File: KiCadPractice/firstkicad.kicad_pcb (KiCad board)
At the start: 2 copper layers, 207 x 115.5 mm, 12 parts, among them Q1 BC337, U1 LM358, U2 LM358

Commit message: Fixed edge-cuts.
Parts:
- removed the U1 at (191.5, 99.5)
- C1: footprint Capacitor_THT:CP_Axial_L30.0mm_D18.0mm_P35.00mm_Horizontal -> Capacitor_SMD:C_1206_3216Metric_Pad1.33x1.80mm_HandSolder
- D1: value D_Photo -> LTR-516AD; footprint Diode_THT:D_A-405_P5.08mm_Vertical_KathodeUp -> Library:LTR-516AD
- Q1: footprint Transformer_THT:Autotransformer_Toroid_1Tap_Horizontal_D10.5mm_Amidon-T37 -> Package_TO_SOT_THT:TO-92_Inline
- R1, R2, R3, R4, R6: footprint Resistor_THT:R_Axial_DIN0204_L3.6mm_D1.6mm_P7.62mm_Horizontal -> Resistor_SMD:R_1206_3216Metric_Pad1.30x1.75mm_HandSolder
- U1: renamed from U2; footprint OptoDevice:Broadcom_APDS-9160-003 -> Package_TO_SOT_SMD:SOT-23-8_Handsoldering
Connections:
- D1 pad 1: 5 -> +5V
- R2 pad 1: 5 -> +5V
- R3 pad 1: 5 -> +5V
- R6 pad 1: 5 -> +5V
- RV1 pad 2: Net-(U2A--) -> Net-(U1B--)
- RV2 pad 2: Net-(U2A-+) -> Net-(U1B-+)
- U1 pad 1: Net-(RV1-Pad3) -> Net-(U1A--)
- U1 pad 2: Net-(U2A--) -> Net-(U1A--)
- U1 pad 3: Net-(U2A-+) -> Net-(U1A-+)
- U1 pad 4: (no net) -> +5V
- U1 pad 5: (no net) -> Net-(U1B-+)
- U1 pad 6: (no net) -> Net-(U1B--)
- U1 pad 7: (no net) -> Net-(RV1-Pad3)
- U1 pad 8: (no net) -> GND
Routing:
- net Net-(U1A--): track 29.4 -> 101.0 mm
- net Net-(U1A-+): track 71.6 -> 0.00 mm
- net Net-(U2A-+): track 69.2 -> 0.00 mm
- net (no net): track 0.00 -> 69.2 mm
- net Net-(U2A--): track 22.3 -> 0.00 mm
- net Net-(U1B--): track 0.00 -> 22.3 mm
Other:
- board size 207 x 115.5 mm -> 196.2 x 103 mm

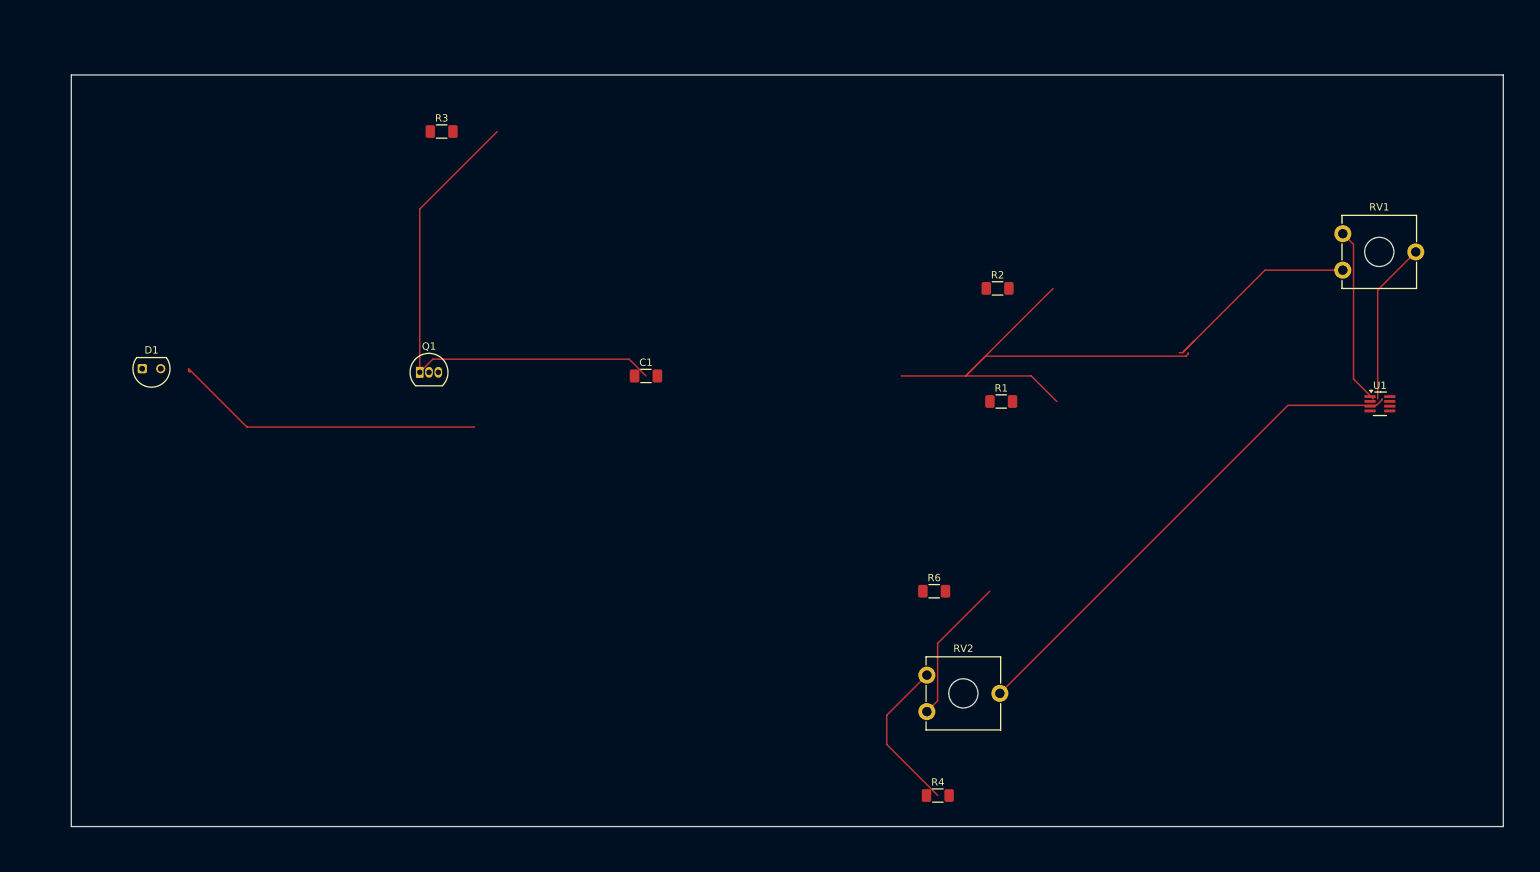
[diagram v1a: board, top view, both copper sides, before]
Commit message: Patched some more footprints.
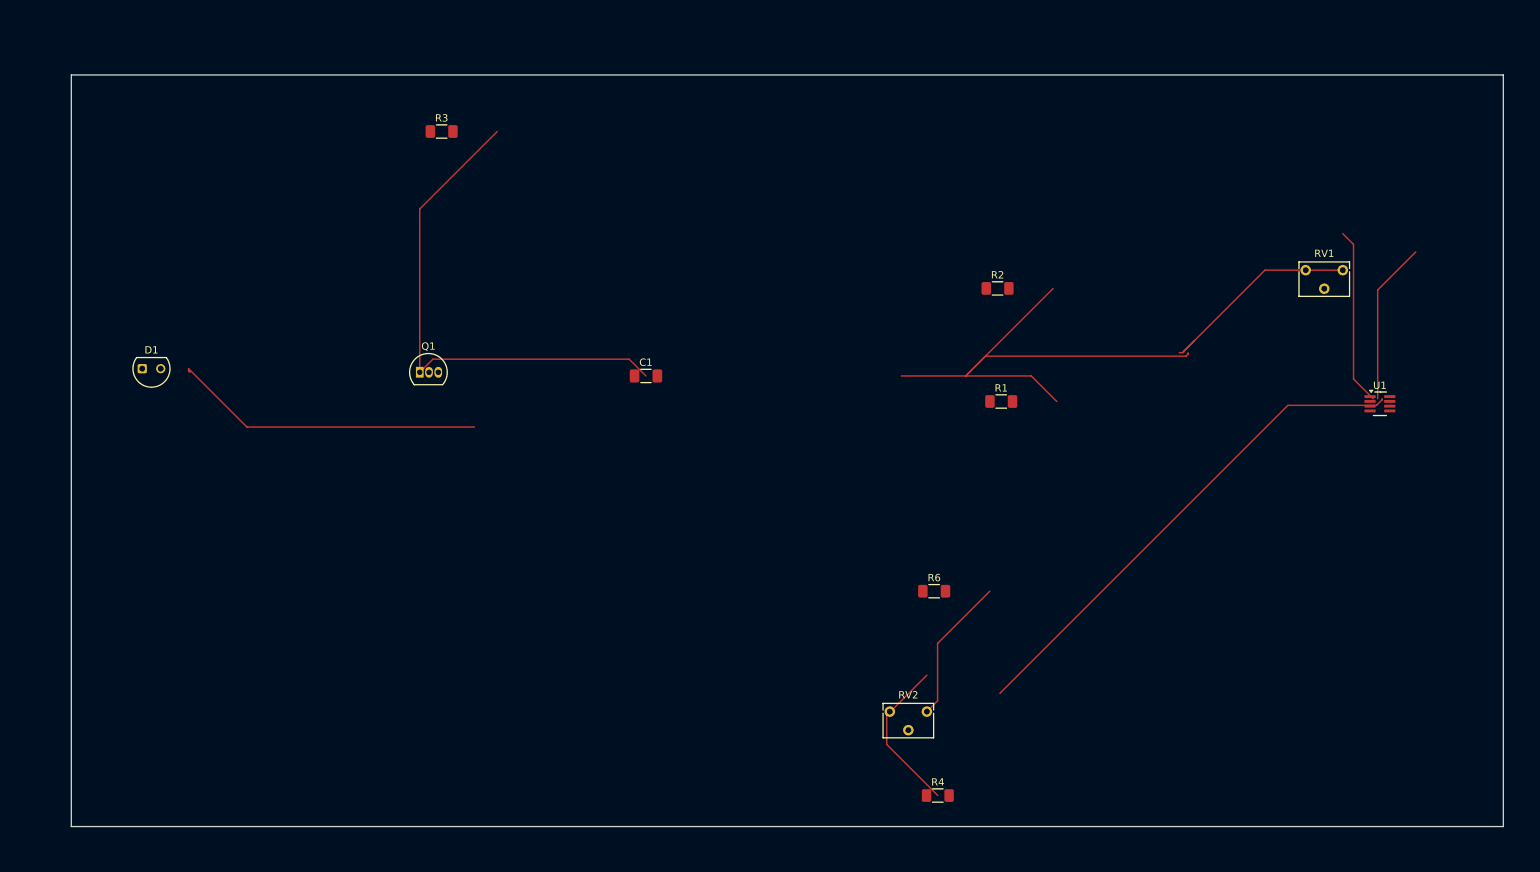
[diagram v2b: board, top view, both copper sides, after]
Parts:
- Q1: footprint Package_TO_SOT_THT:TO-92_Inline -> Package_TO_SOT_THT:TO-92L_Inline
- RV1, RV2: footprint Potentiometer_THT:Potentiometer_ACP_CA9-V10_Vertical_Hole -> Potentiometer_THT:Potentiometer_Bourns_3266W_Vertical
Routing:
- net Net-(U1A-+): track 0.00 -> 69.2 mm
- net (no net): track 69.2 -> 0.00 mm
- net Net-(U1A--): track 101.0 -> 125.4 mm
- net Net-(RV1-Pad3): track 24.3 -> 0.00 mm
